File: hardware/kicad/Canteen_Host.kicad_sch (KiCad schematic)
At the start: 11 parts, among them J2 ST7789 2.8in 320x240, J3 DS3231 ZS-042, J4 Battery 1S Li-ion, SW1 Tactile switch, U1 ESP32-S3-DevKitC-1 N16R8

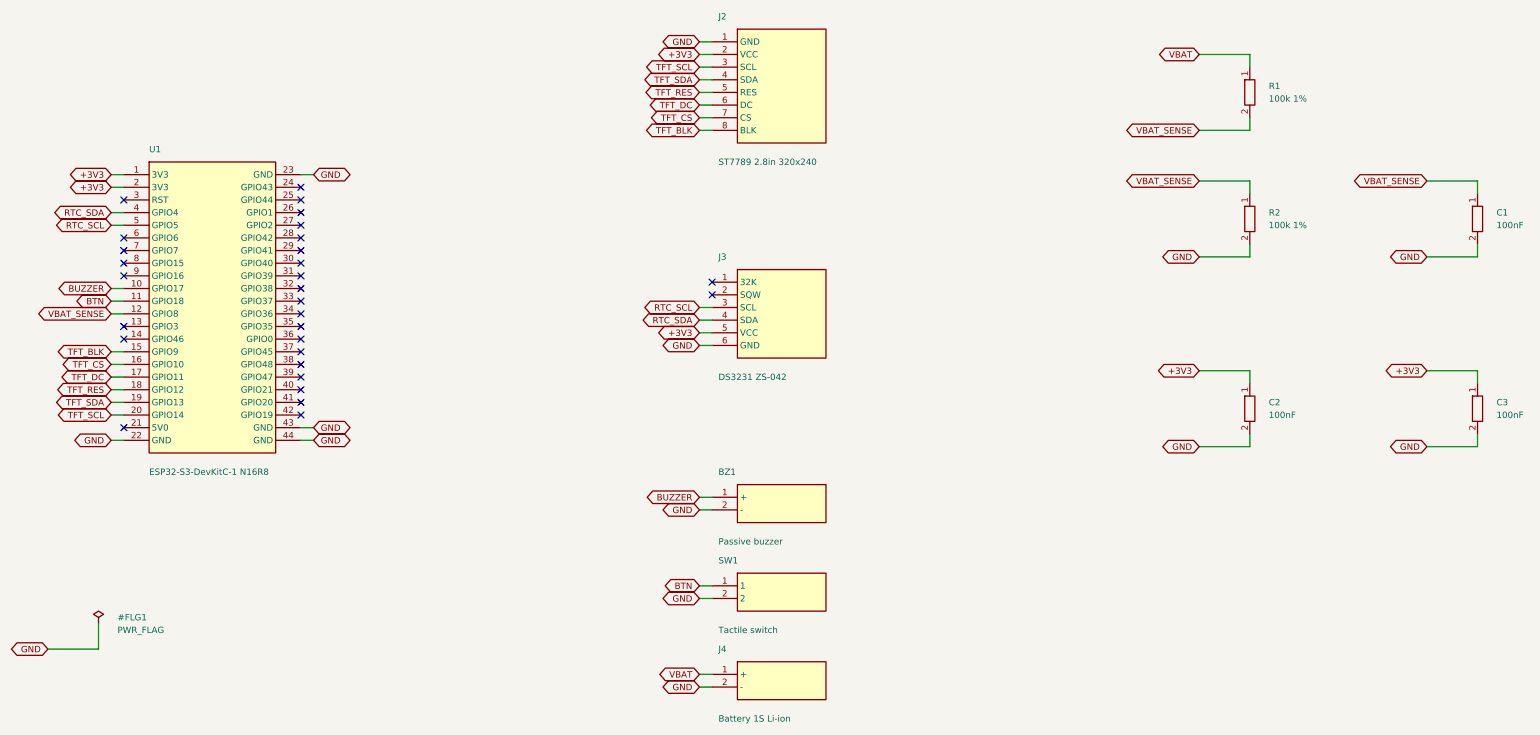
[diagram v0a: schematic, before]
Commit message: บันทึกสำเนาลงการ์ด SD ที่อยู่หลังโมดูลจอ (Host 113.11.0)
หัวต่อการ์ดบนโมดูลจอเป็นคนละชุดกับหัวแถว SPI ของจอ อยู่คนละขอบบอร์ด
ต้องเดินสายเพิ่มสี่เส้น แต่สองเส้นใช้บัสร่วมกับจอได้ คือ SD_SCK ไป GPIO14
เส้นเดียวกับ TFT SCL และ SD_MOSI ไป GPIO13 เส้นเดียวกับ TFT SDA
เหลือ SD_MISO กับ SD_CS ที่ต้องมีขาของตัวเอง ลงตำแหน่ง 6 กับ 7 ที่ว่างอยู่พอดี
สายจึงยังไม่ไขว้กันเหมือนผังเดิม ใช้บัสร่วมกันได้เพราะแยกด้วยขา CS
และจอในผังนี้ไม่ได้ใช้ขา MISO จึงไม่แย่งสายกัน
แก้ SPI_TFT.begin() ให้มี MISO จริง ของเดิมใส่ -1 ไว้เพราะจอไม่ต้องใช้

LittleFS ยังเป็นที่เก็บหลักเหมือนเดิม การ์ดเป็นเพียงสำเนา ตั้งใจออกแบบแบบนี้
เพราะการ์ดถอดออกได้ เสียได้ และไม่มีก็ได้ ถ้าให้การ์ดเป็นที่เก็บหลัก
วันที่ลืมเสียบการ์ดคือวันที่ระบบจ่ายอาหารไม่ได้
เขียนสำเนาสามอย่าง รายการประจำวันทุกครั้งที่รับสิทธิ์สำเร็จ ไฟล์ปิดยอดตอนปิดวัน
และทะเบียนนิสิตทุกครั้งที่เปลี่ยน ถ้าไม่มีการ์ดก็ข้ามไปเฉย ๆ
และลองเมานต์ใหม่ทุกสามสิบวินาที เสียบทีหลังได้โดยไม่ต้องรีบูต
เพิ่มแผงสถานะการ์ดในหน้าตั้งค่าบนเว็บ

processScanRequest() ส่งคำตอบให้จุดบริการก่อนแล้วค่อยเขียนไฟล์อยู่แล้ว
การ์ดที่เขียนช้าจึงไม่ทำให้จุดบริการรอจนหมดเวลา ตรงนี้ไม่ต้องแก้

หลังเพิ่มขา pincheck.py ยังขึ้นว่าผ่านแต่จำนวนขาที่รายงานยังเป็น 12 เท่าเดิม
เพราะ regex จับเฉพาะชื่อที่มีอยู่ตอนเขียน ขาที่ขึ้นต้นด้วย SD_ จึงถูกมองข้ามเงียบ ๆ
เป็นบั๊กชนิดเดียวกับ packetcheck.py รอบก่อน แก้แล้วตอนนี้นับได้ 14 ขาถูกต้อง

เพิ่มสัญลักษณ์หัวต่อการ์ดลงในไฟล์วงจรของแม่ข่าย สร้างใหม่ด้วยสคริปต์
และแก้กติกาของ kicadcheck.py จากเดิมที่บังคับว่าเน็ตสัญญาณต้องมีสองปลายพอดี
เป็นต้องมีอย่างน้อยสองปลาย และถ้าเกินสองต้องอยู่ในรายการบัสที่ใช้ร่วมกัน
ซึ่งเข้มกว่าเดิมเพราะยังจับขาชนกันโดยไม่ตั้งใจได้ พิสูจน์แล้วโดยลองเอา TFT_SCL
ออกจากรายการ ตัวตรวจฟ้องทันที ตัวตรวจทั้งสิบตัวผ่าน

Co-Authored-By: Claude Opus 5 <noreply@anthropic.com>
Claude-Session: https://claude.ai/code/session_01X9SBq9sFrEp9tTPMPW8bbn
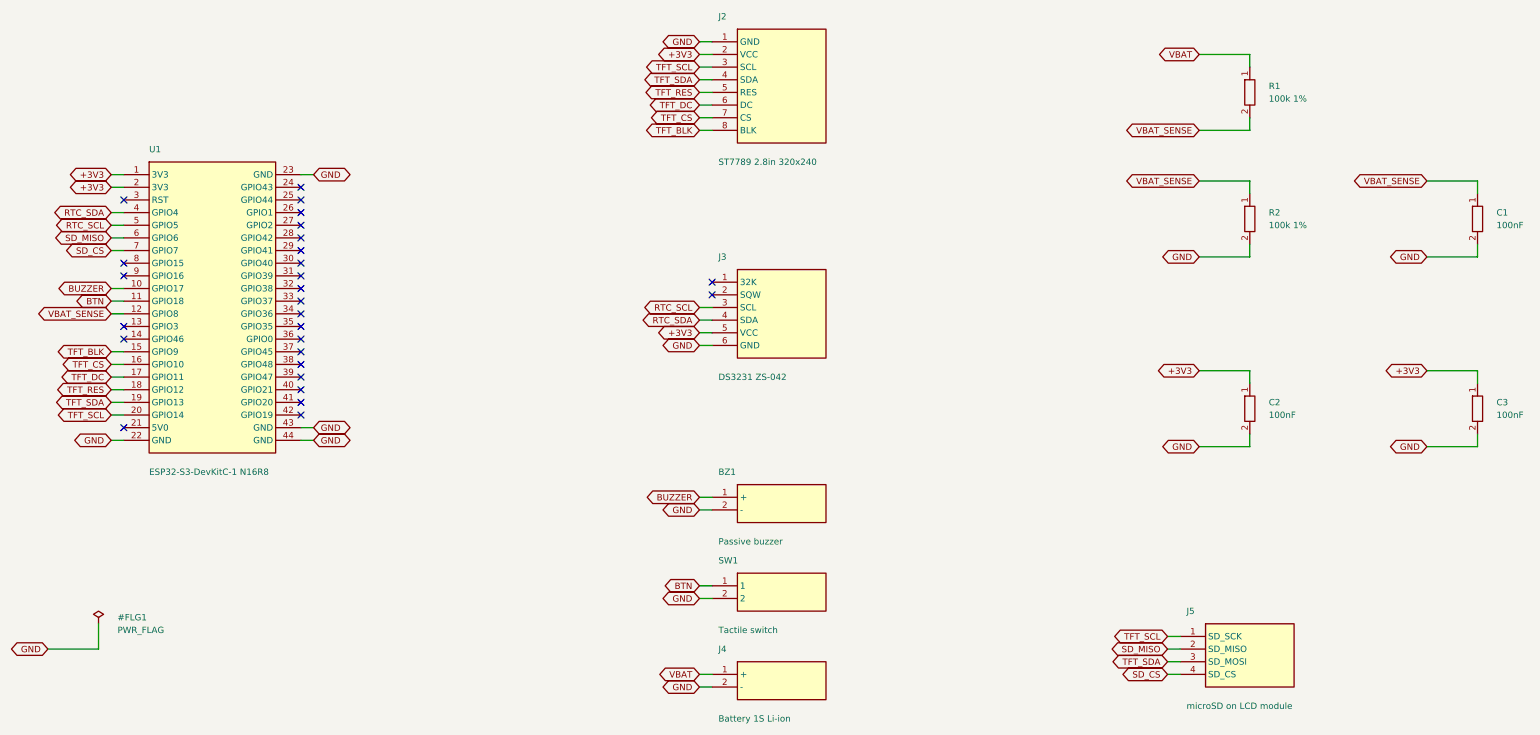
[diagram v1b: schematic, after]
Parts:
- added J5: microSD on LCD module, symbol MCUPR_Canteen:SD_SLOT
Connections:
- net TFT_SCL: now also J5.1 (SD_SCK)
- net TFT_SDA: now also J5.3 (SD_MOSI)
- net SD_MISO: now reaches U1.6 (GPIO6)
- net SD_MISO: now also J5.2 (SD_MISO)
- net SD_CS: now reaches U1.7 (GPIO7)
- net SD_CS: now also J5.4 (SD_CS)
- no-connect marks 29 -> 27
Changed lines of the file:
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@@
     (pin "43")
     (pin "44")
-    (instances (project "Canteen_Host" (path "/0facb458-cc39-4c4e-99fe-ec637f43092e" (reference "U1") (unit 1))))
+    (instances (project "Canteen_Host" (path "/d3199036-6fd6-40f2-83a0-9a5671a86bb7" (reference "U1") (unit 1))))
   )
   (wire (pts (xy 58.42 82.55) (xy 55.88 82.55))
@@
       (effects (font (size 1.27 1.27)) hide))
   )
-  (no_connect (at 58.42 95.25))
-  (no_connect (at 58.42 97.79))
+  (wire (pts (xy 58.42 95.25) (xy 55.88 95.25))
+    (stroke (width 0) (type default))
+  )
+  (global_label "SD_MISO" (shape bidirectional) (at 55.88 95.25 180) (fields_autoplaced)
+    (effects (font (size 1.27 1.27)) (justify right))
+    (property "Intersheetrefs" "${INTERSHEET_REFS}" (at 0 0 0)
+      (effects (font (size 1.27 1.27)) hide))
+  )
+  (wire (pts (xy 58.42 97.79) (xy 55.88 97.79))
+    (stroke (width 0) (type default))
+  )
+  (global_label "SD_CS" (shape bidirectional) (at 55.88 97.79 180) (fields_autoplaced)
+    (effects (font (size 1.27 1.27)) (justify right))
+    (property "Intersheetrefs" "${INTERSHEET_REFS}" (at 0 0 0)
+      (effects (font (size 1.27 1.27)) hide))
+  )
   (no_connect (at 58.42 100.33))
   (no_connect (at 58.42 102.87))
@@
     (pin "7")
     (pin "8")
-    (instances (project "Canteen_Host" (path "/0facb458-cc39-4c4e-99fe-ec637f43092e" (reference "J2") (unit 1))))
+    (instances (project "Canteen_Host" (path "/d3199036-6fd6-40f2-83a0-9a5671a86bb7" (reference "J2") (unit 1))))
   )
   (wire (pts (xy 176.53 55.88) (xy 173.99 55.88))
@@
     (pin "5")
     (pin "6")
-    (instances (project "Canteen_Host" (path "/0facb458-cc39-4c4e-99fe-ec637f43092e" (reference "J3") (unit 1))))
+    (instances (project "Canteen_Host" (path "/d3199036-6fd6-40f2-83a0-9a5671a86bb7" (reference "J3") (unit 1))))
   )
   (no_connect (at 176.53 104.14))
@@
       (effects (font (size 1.27 1.27)) hide))
   )
+  (symbol (lib_id "MCUPR_Canteen:SD_SLOT") (at 284.48 175.26 0) (unit 1)
+    (in_bom yes) (on_board yes) (dnp no) (fields_autoplaced)
+    (property "Reference" "J5" (at 271.78 170.18 0) (effects (font (size 1.27 1.27)) (justify left)))
+    (property "Value" "microSD on LCD module" (at 271.78 189.23 0) (effects (font (size 1.27 1.27)) (justify left)))
+    (property "Footprint" "" (at 0 0 0) (effects (font (size 1.27 1.27)) hide))
+    (property "Datasheet" "" (at 0 0 0) (effects (font (size 1.27 1.27)) hide))
+    (pin "1")
+    (pin "2")
+    (pin "3")
+    (pin "4")
+    (instances (project "Canteen_Host" (path "/d3199036-6fd6-40f2-83a0-9a5671a86bb7" (reference "J5") (unit 1))))
+  )
+  (wire (pts (xy 270.51 175.26) (xy 267.97 175.26))
+    (stroke (width 0) (type default))
+  )
+  (global_label "TFT_SCL" (shape bidirectional) (at 267.97 175.26 180) (fields_autoplaced)
+    (effects (font (size 1.27 1.27)) (justify right))
+    (property "Intersheetrefs" "${INTERSHEET_REFS}" (at 0 0 0)
+      (effects (font (size 1.27 1.27)) hide))
+  )
+  (wire (pts (xy 270.51 177.80) (xy 267.97 177.80))
+    (stroke (width 0) (type default))
+  )
+  (global_label "SD_MISO" (shape bidirectional) (at 267.97 177.80 180) (fields_autoplaced)
+    (effects (font (size 1.27 1.27)) (justify right))
+    (property "Intersheetrefs" "${INTERSHEET_REFS}" (at 0 0 0)
+      (effects (font (size 1.27 1.27)) hide))
+  )
+  (wire (pts (xy 270.51 180.34) (xy 267.97 180.34))
+    (stroke (width 0) (type default))
+  )
+  (global_label "TFT_SDA" (shape bidirectional) (at 267.97 180.34 180) (fields_autoplaced)
+    (effects (font (size 1.27 1.27)) (justify right))
+    (property "Intersheetrefs" "${INTERSHEET_REFS}" (at 0 0 0)
+      (effects (font (size 1.27 1.27)) hide))
+  )
+  (wire (pts (xy 270.51 182.88) (xy 267.97 182.88))
+    (stroke (width 0) (type default))
+  )
+  (global_label "SD_CS" (shape bidirectional) (at 267.97 182.88 180) (fields_autoplaced)
+    (effects (font (size 1.27 1.27)) (justify right))
+    (property "Intersheetrefs" "${INTERSHEET_REFS}" (at 0 0 0)
+      (effects (font (size 1.27 1.27)) hide))
+  )
   (symbol (lib_id "MCUPR_Canteen:BUZZER") (at 190.50 147.32 0) (unit 1)
     (in_bom yes) (on_board yes) (dnp no) (fields_autoplaced)
@@
     (pin "1")
     (pin "2")
-    (instances (project "Canteen_Host" (path "/0facb458-cc39-4c4e-99fe-ec637f43092e" (reference "BZ1") (unit 1))))
+    (instances (project "Canteen_Host" (path "/d3199036-6fd6-40f2-83a0-9a5671a86bb7" (reference "BZ1") (unit 1))))
   )
   (wire (pts (xy 176.53 147.32) (xy 173.99 147.32))
@@
     (pin "1")
     (pin "2")
-    (instances (project "Canteen_Host" (path "/0facb458-cc39-4c4e-99fe-ec637f43092e" (reference "SW1") (unit 1))))
+    (instances (project "Canteen_Host" (path "/d3199036-6fd6-40f2-83a0-9a5671a86bb7" (reference "SW1") (unit 1))))
   )
   (wire (pts (xy 176.53 165.10) (xy 173.99 165.10))
@@
     (pin "1")
     (pin "2")
-    (instances (project "Canteen_Host" (path "/0facb458-cc39-4c4e-99fe-ec637f43092e" (reference "J4") (unit 1))))
+    (instances (project "Canteen_Host" (path "/d3199036-6fd6-40f2-83a0-9a5671a86bb7" (reference "J4") (unit 1))))
   )
   (wire (pts (xy 176.53 182.88) (xy 173.99 182.88))
@@
     (pin "1")
     (pin "2")
-    (instances (project "Canteen_Host" (path "/0facb458-cc39-4c4e-99fe-ec637f43092e" (reference "R1") (unit 1))))
+    (instances (project "Canteen_Host" (path "/d3199036-6fd6-40f2-83a0-9a5671a86bb7" (reference "R1") (unit 1))))
   )
   (wire (pts (xy 284.48 60.96) (xy 284.48 58.42))
@@
     (pin "1")
     (pin "2")
-    (instances (project "Canteen_Host" (path "/0facb458-cc39-4c4e-99fe-ec637f43092e" (reference "R2") (unit 1))))
+    (instances (project "Canteen_Host" (path "/d3199036-6fd6-40f2-83a0-9a5671a86bb7" (reference "R2") (unit 1))))
   )
   (wire (pts (xy 284.48 86.36) (xy 284.48 83.82))
@@
     (pin "1")
     (pin "2")
-    (instances (project "Canteen_Host" (path "/0facb458-cc39-4c4e-99fe-ec637f43092e" (reference "C1") (unit 1))))
+    (instances (project "Canteen_Host" (path "/d3199036-6fd6-40f2-83a0-9a5671a86bb7" (reference "C1") (unit 1))))
   )
   (wire (pts (xy 330.20 86.36) (xy 330.20 83.82))
@@
     (pin "1")
     (pin "2")
-    (instances (project "Canteen_Host" (path "/0facb458-cc39-4c4e-99fe-ec637f43092e" (reference "C2") (unit 1))))
+    (instances (project "Canteen_Host" (path "/d3199036-6fd6-40f2-83a0-9a5671a86bb7" (reference "C2") (unit 1))))
   )
   (wire (pts (xy 284.48 124.46) (xy 284.48 121.92))
@@
     (pin "1")
     (pin "2")
-    (instances (project "Canteen_Host" (path "/0facb458-cc39-4c4e-99fe-ec637f43092e" (reference "C3") (unit 1))))
+    (instances (project "Canteen_Host" (path "/d3199036-6fd6-40f2-83a0-9a5671a86bb7" (reference "C3") (unit 1))))
   )
   (wire (pts (xy 330.20 124.46) (xy 330.20 121.92))
@@
     (property "Datasheet" "" (at 0 0 0) (effects (font (size 1.27 1.27)) hide))
     (pin "1")
-    (instances (project "Canteen_Host" (path "/0facb458-cc39-4c4e-99fe-ec637f43092e" (reference "#FLG1") (unit 1))))
+    (instances (project "Canteen_Host" (path "/d3199036-6fd6-40f2-83a0-9a5671a86bb7" (reference "#FLG1") (unit 1))))
   )
   (wire (pts (xy 53.34 172.72) (xy 53.34 177.80))
